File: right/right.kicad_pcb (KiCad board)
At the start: 2 copper layers, 117.6 x 97.9 mm, 53 parts, among them J2 USB_C_Receptacle_OUT, SW1 SW_Push, SW2 SW_SPDT, U1 STM32G0B1CBTx, U2 SRV05-4, U3 XC6206P332MR, U4 FSUSB42MUX

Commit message: finished modifying right side
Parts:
- J2, R1, SW1, SW2: moved to B.Cu
- KEY1, KEY10, KEY11, KEY12, KEY13, KEY14, KEY15, KEY16, KEY17, KEY2, KEY3, KEY4, KEY5, KEY6, KEY7, KEY8, KEY9: footprint Keyswitches Marbastlib:SW_choc_v1_HS_CPG135001S30_1u -> marbastlib-choc:SW_choc_v1_HS_CPG135001S30_1u
- moved R2 8.95 mm to (84.2, 115.0)
- moved R3 8.41 mm to (83.8, 121.7), turned to -90 degrees
- moved D18 2.95 mm to (82.0, 127.7), turned to 180 degrees
- moved F2 1.05 mm to (80.2, 124.7)
- moved J2 0.59 mm to (76.8, 118.0), turned to 90 degrees
- turned SW2 to 180 degrees
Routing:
- net +3.3V: track 98.2 -> 92.0 mm, vias 1 -> 0
- net nRST: track 31.8 -> 27.1 mm, vias 3 -> 2
- net Net-(J2-CC1): track 7.02 -> 3.48 mm, vias 1 -> 0
- net USB_D+: track 35.9 -> 39.0 mm, vias 1 -> 0
- net VBUS: track 13.3 -> 15.8 mm, vias 1 -> 0
- net SEL: track 45.9 -> 44.2 mm, vias 3 -> 2
- net Net-(J2-CC2): track 5.84 -> 4.81 mm, vias 1 -> 0
- net Net-(D18-A): track 4.71 -> 3.85 mm
- net USB_D-: track 36.1 -> 36.9 mm, vias 2 -> 3
- net COL3: track 86.3 -> 85.6 mm
- net GND: track 14.9 -> 14.6 mm, vias 33 -> 39
- net BOOT0: track 30.1 -> 30.2 mm, vias 3 -> 4
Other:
- outline, holes or cut-outs redrawn
- board text added: "{dblquote}You'd be able to if you were black{dblquote}"
- board text removed: "I was pointing to a camera or a speaker I swear"

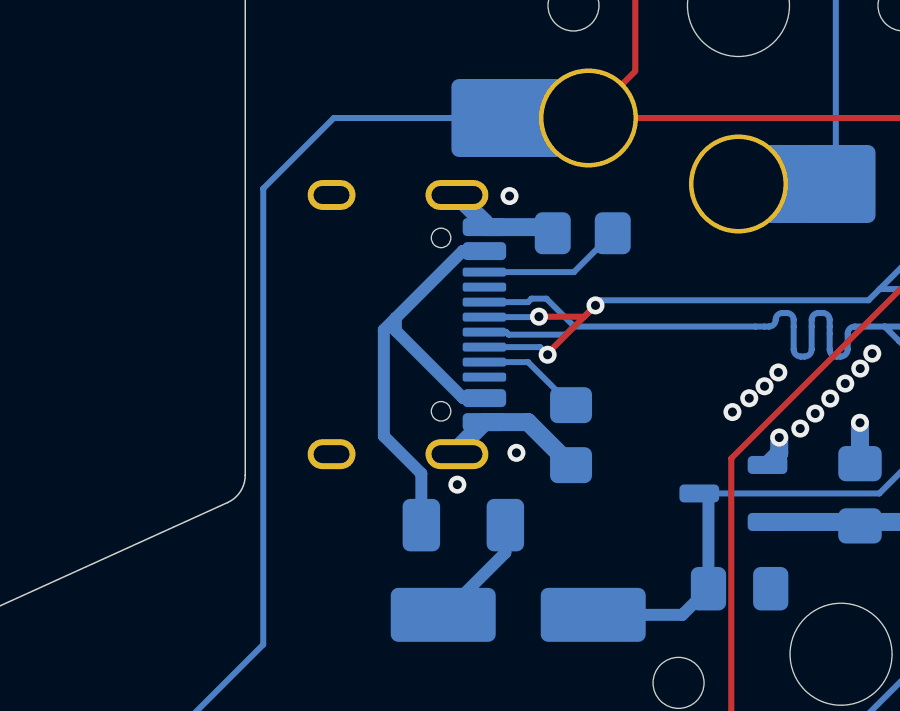
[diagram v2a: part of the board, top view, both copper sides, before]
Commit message: pushed usb a bit outwards for better fitting with the case
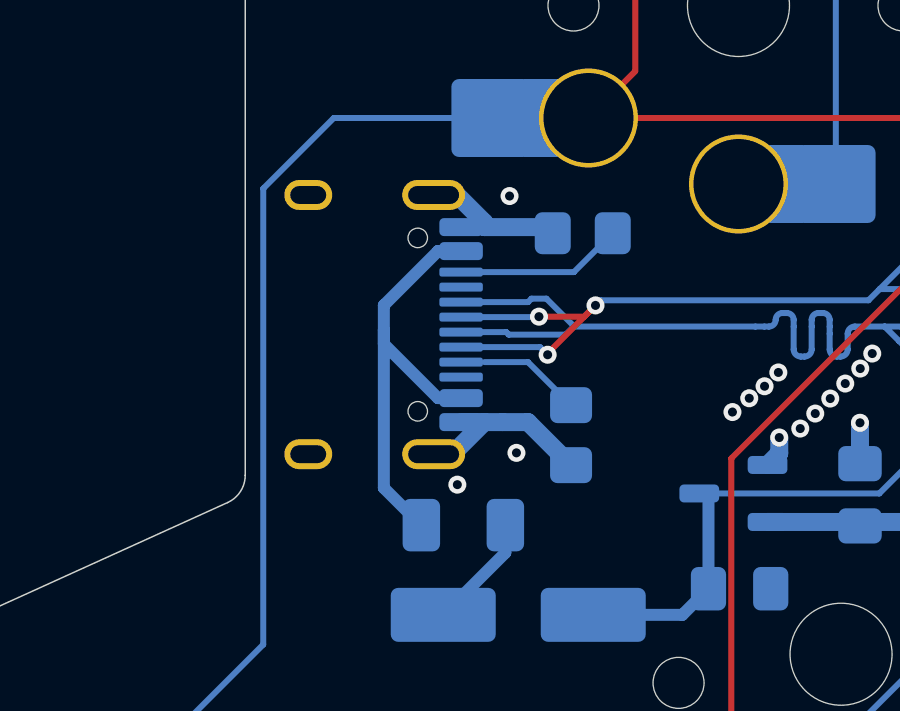
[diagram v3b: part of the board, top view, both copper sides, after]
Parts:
- moved J2 0.78 mm to (76.0, 118.0)
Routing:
- net USB_D-: track 36.9 -> 38.5 mm
- net USB_D+: track 39.0 -> 40.5 mm
- net Net-(J2-CC2): track 4.81 -> 5.59 mm
- net GND: track 14.6 -> 15.4 mm
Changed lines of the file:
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@@
 		(descr "Hotswap footprint for Kailh Choc style switches")
 		(property "Reference" "KEY11"
-			(at 5 -7.4 0)
+			(at -4.699041 -3.511689 0)
 			(layer "B.SilkS")
 			(effects
@@
 	(footprint "Connector_USB:USB_C_Receptacle_HRO_TYPE-C-31-M-12"
 		(layer "B.Cu")
-		(at 76.827064 118.035 90)
+		(at 76.05 118.035 90)
 		(descr "USB Type-C receptacle for USB 2.0 and PD, http://www.krhro.com/uploads/soft/180320/1-1P320120243.pdf")
 		(tags "usb usb-c 2.0 pd")
@@
 	(segment
 		(start 80.872064 121.285)
-		(end 82.325 121.285)
+		(end 81.48 121.285)
 		(width 0.6)
 		(layer "B.Cu")
@@
 	)
 	(segment
+		(start 80.872064 121.285)
+		(end 80.095 121.285)
+		(width 0.6)
+		(layer "B.Cu")
+		(net "GND")
+	)
+	(segment
 		(start 79.957064 122.355)
 		(end 79.957064 122.2)
@@
 	)
 	(segment
+		(start 81.48 121.285)
+		(end 82.325 121.285)
+		(width 0.6)
+		(layer "B.Cu")
+		(net "GND")
+	)
+	(segment
 		(start 80.872064 114.785)
 		(end 80.872064 114.63)
@@
 	)
 	(segment
-		(start 82.441471 117.17)
-		(end 82.938529 117.17)
-		(width 0.2)
-		(layer "B.Cu")
-		(net "USB_D+")
-	)
-	(segment
 		(start 94.2125 118.1)
 		(end 93.22025 118.1)
@@
 	)
 	(segment
-		(start 80.872064 118.285)
-		(end 81.6 118.285)
+		(start 82.326471 117.285)
+		(end 82.441471 117.17)
 		(width 0.2)
 		(layer "B.Cu")
@@
 	)
 	(segment
+		(start 83.58 118.37)
+		(end 83.85 118.1)
+		(width 0.2)
+		(layer "B.Cu")
+		(net "USB_D+")
+	)
+	(segment
+		(start 83.85 118.1)
+		(end 83.868529 118.1)
+		(width 0.2)
+		(layer "B.Cu")
+		(net "USB_D+")
+	)
+	(segment
 		(start 94.2125 118.1)
 		(end 94.7625 118.1)
@@
 	)
 	(segment
-		(start 94.9625 118.3)
-		(end 96.974999 118.3)
+		(start 80.095 118.285)
+		(end 81.6 118.285)
 		(width 0.2)
 		(layer "B.Cu")
@@
 	)
 	(segment
-		(start 83.58 118.37)
-		(end 83.85 118.1)
+		(start 94.9625 118.3)
+		(end 96.974999 118.3)
 		(width 0.2)
 		(layer "B.Cu")
@@
 	)
 	(segment
-		(start 80.872064 117.285)
-		(end 82.326471 117.285)
-		(width 0.2)
-		(layer "B.Cu")
-		(net "USB_D+")
-	)
-	(segment
 		(start 92.38025 118.34)
 		(end 92.38025 118.1)
@@
 	)
 	(segment
-		(start 82.326471 117.285)
-		(end 82.441471 117.17)
+		(start 96.974999 118.3)
+		(end 97.7 118.3)
 		(width 0.2)
 		(layer "B.Cu")
@@
 	)
 	(segment
-		(start 82.938529 117.17)
-		(end 83.868529 118.1)
+		(start 81.685 118.37)
+		(end 83.58 118.37)
 		(width 0.2)
 		(layer "B.Cu")
@@
 	)
 	(segment
-		(start 96.974999 118.3)
-		(end 97.7 118.3)
+		(start 82.938529 117.17)
+		(end 83.868529 118.1)
 		(width 0.2)
 		(layer "B.Cu")
@@
 	)
 	(segment
-		(start 83.85 118.1)
-		(end 83.868529 118.1)
+		(start 80.095 117.285)
+		(end 82.326471 117.285)
 		(width 0.2)
 		(layer "B.Cu")
@@
 	)
 	(segment
-		(start 81.6 118.285)
-		(end 81.685 118.37)
+		(start 82.441471 117.17)
+		(end 82.938529 117.17)
 		(width 0.2)
 		(layer "B.Cu")
@@
 	)
 	(segment
-		(start 81.685 118.37)
-		(end 83.58 118.37)
+		(start 81.6 118.285)
+		(end 81.685 118.37)
 		(width 0.2)
 		(layer "B.Cu")
@@
 	)
 	(segment
-		(start 80.872064 118.785)
-		(end 82.725 118.785)
-		(width 0.2)
-		(layer "B.Cu")
-		(net "USB_D-")
-	)
-	(segment
 		(start 97.2 115.4)
 		(end 103.6 121.8)
@@
 	)
 	(segment
-		(start 82.725 118.785)
-		(end 82.98 119.04)
+		(start 82.98 119.04)
+		(end 82.725 118.785)
 		(width 0.2)
 		(layer "B.Cu")
@@
 	)
 	(segment
-		(start 94.05 116.85)
-		(end 95.5 115.4)
+		(start 82.725 118.785)
+		(end 80.095 118.785)
 		(width 0.2)
 		(layer "B.Cu")
@@
 	)
 	(segment
-		(start 103.6 121.8)
-		(end 107.8 121.8)
+		(start 94.05 116.85)
+		(end 95.5 115.4)
 		(width 0.2)
 		(layer "B.Cu")
@@
 	)
 	(segment
-		(start 82.675 117.785)
-		(end 82.69 117.77)
+		(start 103.6 121.8)
+		(end 107.8 121.8)
 		(width 0.2)
 		(layer "B.Cu")
@@
 	)
 	(segment
-		(start 80.872064 117.785)
-		(end 82.675 117.785)
+		(start 82.675 117.785)
+		(end 80.095 117.785)
 		(width 0.2)
 		(layer "B.Cu")
@@
 	)
 	(segment
+		(start 82.69 117.77)
+		(end 82.675 117.785)
+		(width 0.2)
+		(layer "B.Cu")
+		(net "USB_D-")
+	)
+	(segment
 		(start 93.675 117.225)
 		(end 84.745 117.225)
@@
 	)
 	(segment
-		(start 77.52 118.21)
-		(end 77.52 118.24)
-		(width 0.4)
-		(layer "B.Cu")
-		(net "VBUS")
-	)
-	(segment
-		(start 77.92 117.81)
-		(end 77.52 118.21)
+		(start 80.175 115.585)
+		(end 79.325 115.585)
 		(width 0.4)
 		(layer "B.Cu")
@@
 	)
 	(segment
-		(start 80.165 120.485)
-		(end 80.872064 120.485)
+		(start 79.325 115.585)
+		(end 80.095 115.585)
 		(width 0.4)
 		(layer "B.Cu")
@@
 	)
 	(segment
-		(start 77.92 118.24)
-		(end 80.165 120.485)
+		(start 77.52 118.21)
+		(end 77.52 118.68)
 		(width 0.4)
 		(layer "B.Cu")
@@
 	)
 	(segment
-		(start 80.175 115.585)
-		(end 80.145 115.585)
+		(start 77.52 117.39)
+		(end 77.52 118.21)
 		(width 0.4)
 		(layer "B.Cu")
@@
 	)
 	(segment
-		(start 80.872064 115.585)
-		(end 80.175 115.585)
+		(start 78.76 124.72)
+		(end 78.77 124.72)
 		(width 0.4)
 		(layer "B.Cu")
@@
 	)
 	(segment
-		(start 77.92 118.24)
-		(end 77.92 117.81)
+		(start 79.325 115.585)
+		(end 77.52 117.39)
 		(width 0.4)
 		(layer "B.Cu")
@@
 	)
 	(segment
-		(start 78.77 123)
-		(end 78.77 124.72)
+		(start 77.52 118.21)
+		(end 77.52 123.48)
 		(width 0.4)
 		(layer "B.Cu")
@@
 	)
 	(segment
-		(start 77.52 118.24)
-		(end 77.52 121.75)
+		(start 77.52 118.68)
+		(end 79.325 120.485)
 		(width 0.4)
 		(layer "B.Cu")
@@
 	)
 	(segment
-		(start 80.145 115.585)
-		(end 77.92 117.81)
+		(start 79.325 120.485)
+		(end 80.095 120.485)
 		(width 0.4)
 		(layer "B.Cu")
@@
 	)
 	(segment
-		(start 77.52 121.75)
-		(end 78.77 123)
+		(start 77.52 123.48)
+		(end 78.76 124.72)
 		(width 0.4)
 		(layer "B.Cu")
@@
 	)
 	(segment
-		(start 80.872064 116.285)
+		(start 85.15 114.99)
 		(end 83.855 116.285)
 		(width 0.2)
@@
 	(segment
 		(start 83.855 116.285)
-		(end 85.15 114.99)
+		(end 80.095 116.285)
 		(width 0.2)
 		(layer "B.Cu")
